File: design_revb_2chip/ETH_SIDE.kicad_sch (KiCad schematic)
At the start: 1 part, among them U2 DP83TG720SWRHARQ1

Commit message: finished initial schematic
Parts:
- added C10, C13, C21, C22, C28: 100nF, symbol Device:C
- added C11, C14, C23, C24, C30: 10nF, symbol Device:C
- added C12, C19, C20, C26: 2.2uF, symbol Device:C
- added C15, C18, C25, C9: 1uF, symbol Device:C
- added C16, C17: 10uF, symbol Device:C
- added C27, C29: 0.1uF, symbol Device:C
- added C31: 4.7nF, symbol Device:C
- added D1, D2, D3: LED, symbol Device:LED
- added FL1, FL2, FL3: BLM18KG601SH1D, BLM18KG601SH1D:BEADC1608X95N, symbol Capstone_Synbols:BLM18KG601SH1D
- added FL4: DLW32MH101XT2L, DLW32MH101XT2L:FIL_DLW32MH101XT2L, symbol Capstone_Synbols:DLW32MH101XT2L
- added J2: 09452812810, 09452812810, symbol Capstone_Synbols:09452812810
- added JP1, JP2, JP5: Jumper_2_Open, symbol Jumper:Jumper_2_Open
- added JP3, JP4: Jumper_2_Bridged, symbol Jumper:Jumper_2_Bridged
- added R10, R11, R12, R14, R15, R18: 2.49k, symbol Device:R_US
- added R13, R16, R17: 470, symbol Device:R_US
- added R5: 10k, symbol Device:R_US
- added R6, R7: 1k, symbol Device:R_US
- added R8: 100k, symbol Device:R_US
- added R9: 2.2k, symbol Device:R_US
- added U5: TPS784105QWDRBRQ1, DRB0008J-IPC_A, symbol Capstone_Synbols:TPS784105QWDRBRQ1
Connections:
- net MDC: now reaches U2.1
- net at U2.10: now also R5.1
- net Vdda3p3: now reaches U2.11
- net Vdda3p3: now also U2.7, U2.8, C26.2, C28.2, C30.2, FL3.2
- net TRD_P: now reaches U2.12
- net TRD_P: now also FL4.1
- net TRD_M: now reaches U2.13
- net TRD_M: now also FL4.4
- net RX_CTRL: now reaches U2.15
- net Vdd1p0A: now reaches U2.21
- net Vdd1p0A: now also U2.9, C19.2, C20.1, C21.2, C22.1, C23.2, C24.1, FL2.2
- net VddioA: now reaches U2.22
- net VddioA: now also U2.34, C10.1, C11.1, C12.2, C13.2, C14.2, FL1.2
- net RX_D3: now reaches U2.23
- net RX_D2: now reaches U2.24
- net RX_D2: now also JP3.1 (A)
- net RX_D1: now reaches U2.25
- net RX_D1: now also JP2.1 (A)
- net RX_D0: now reaches U2.26
- net RX_D0: now also JP1.1 (A)
- net RX_CLK: now reaches U2.27
- net TX_CLK: now reaches U2.28
- net TX_CTRL: now reaches U2.29
- net TX_D3: now reaches U2.30
- net TX_D2: now reaches U2.31
- net TX_D1: now reaches U2.32
- net TX_D0: now reaches U2.33
- net LED_0: now reaches U2.35
- net LED_0: now also JP4.1 (A), JP5.1 (A)
- net MDIO: now reaches U2.36
- net MDIO: now also R9.2
- net CLK_IN: now reaches U2.5
- net LED_1: now reaches U2.6
- net LED_1: now also D3.2 (A), R18.1
- new net: D1.2 (A), JP4.2 (B), R14.1
- new net: JP3.2 (B), R12.2
- new net: C27.1, FL4.2
- new net: C27.2, J2.1 (BI_DA+), R6.1
- new net: D3.1 (K), R17.2
- new net: JP1.2 (B), R10.2
- new net: D2.1 (K), JP5.2 (B), R15.1
- new net: D2.2 (A), R16.1
- new net: C29.1, J2.2 (BI_DA-), R7.1
- new net: C31.1, R6.2, R7.2, R8.1
- new net: JP2.2 (B), R11.2
- new net: C29.2, FL4.3
- new net: D1.1 (K), R13.2
- new net GND: C10.2, C11.2, C12.1, C13.1, C14.1, C15.1, C16.1, C17.1, C18.2, C19.1, C20.2, C21.1, C22.2, C23.1, C24.2, C25.2, C26.1, C28.1, C30.1, C31.2, C9.2, J2.3 (GND_1), J2.4 (GND_2), J2.5 (GND_3), J2.6 (GND_4), R13.1, R14.2, R17.1, R18.2, R5.2, R8.2, R9.1, U5.5 (GND)
- new net Vdd: C15.2, C17.2, C25.1, C9.1, FL1.1, FL3.1, R10.1, R11.1, R12.1, R15.2, R16.2, U5.6 (EN), U5.8 (IN)
- new net Vdd1.0: C16.2, C18.1, FL2.1, U5.1 (OUT)
- no-connect marks 0 -> 13
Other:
- moved on the sheet: U2

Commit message: ready to merge
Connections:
- net GND: now also U2.37
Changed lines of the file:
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@@
+	)
+	(symbol
+		(lib_id "power:GND")
+		(at 77.47 30.48 90)
+		(unit 1)
+		(exclude_from_sim no)
+		(in_bom yes)
+		(on_board yes)
+		(dnp no)
+		(fields_autoplaced yes)
+		(property "Reference" "#PWR044"
+			(at 83.82 30.48 0)
+			(effects
+				(font
+					(size 1.27 1.27)
+				)
+				(hide yes)
+			)
+		)
+		(property "Value" "GND"
+			(at 81.28 30.4799 90)
+			(effects
+				(font
+					(size 1.27 1.27)
+				)
+				(justify right)
+			)
+		)
+		(property "Footprint" ""
+			(at 77.47 30.48 0)
+			(effects
+				(font
+					(size 1.27 1.27)
+				)
+				(hide yes)
+			)
+		)
+		(property "Datasheet" ""
+			(at 77.47 30.48 0)
+			(effects
+				(font
+					(size 1.27 1.27)
+				)
+				(hide yes)
+			)
+		)
+		(property "Description" "Power symbol creates a global label with name \"GND\" , ground"
+			(at 77.47 30.48 0)
+			(effects
+				(font
+					(size 1.27 1.27)
+				)
+				(hide yes)
+			)
+		)
+		(pin "1"
+		)
+		(instances
+			(project ""
+				(path "/d77d37fa-bfdc-44bb-83cc-90773a88d214/0a9cb67f-25c5-4666-b67f-a9781d94061d"
+					(reference "#PWR044")
+					(unit 1)
+				)
+			)
+		)
 	)
 	(symbol

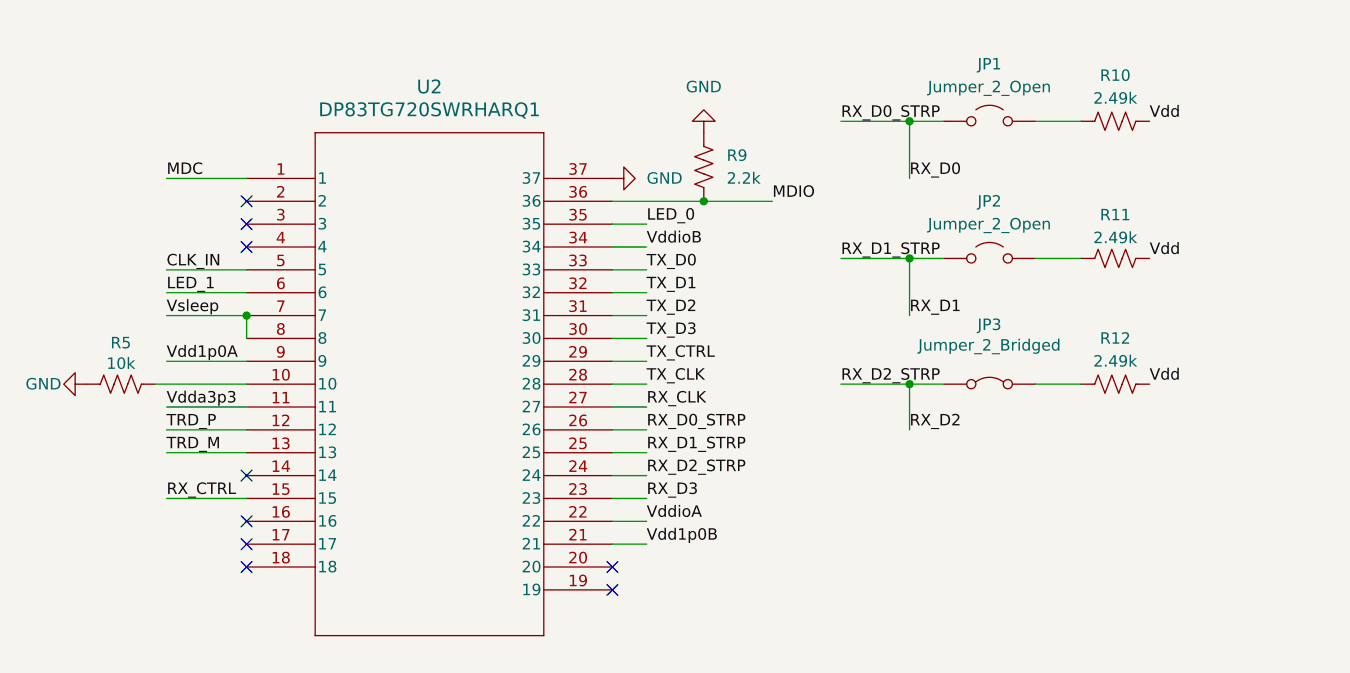
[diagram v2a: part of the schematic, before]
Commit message: Small Fixes
Modifying both pages to try and resolve differences in pins
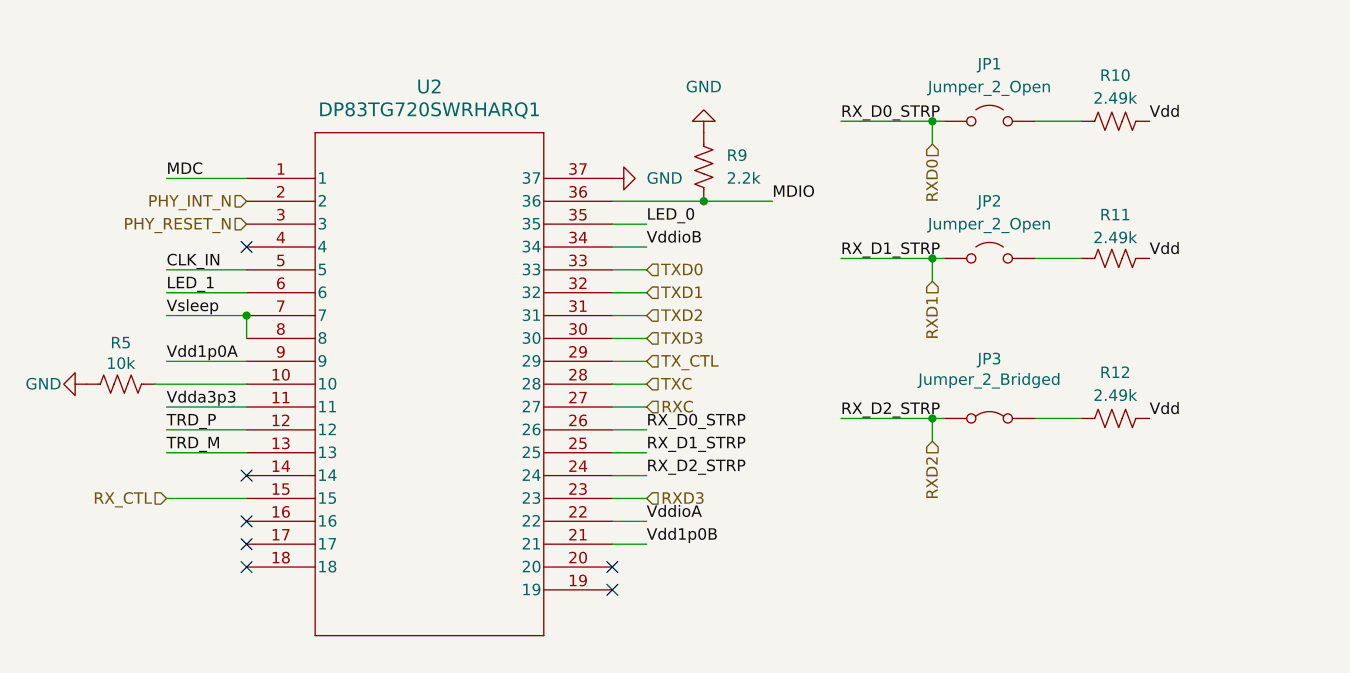
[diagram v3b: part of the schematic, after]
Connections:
- net PHY_INT_N: now reaches U2.2
- net PHY_RESET_N: now reaches U2.3
- net RX_CLK renamed RXC
- net RX_CTRL renamed RX_CTL
- net RX_D0 renamed RXD0
- net RX_D1 renamed RXD1
- net RX_D2 renamed RXD2
- net RX_D3 renamed RXD3
- net TX_CLK renamed TXC
- net TX_CTRL renamed TX_CTL
- net TX_D0 renamed TXD0
- net TX_D1 renamed TXD1
- net TX_D2 renamed TXD2
- net TX_D3 renamed TXD3
- no-connect marks 13 -> 11
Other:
- moved on the sheet: JP3, R12

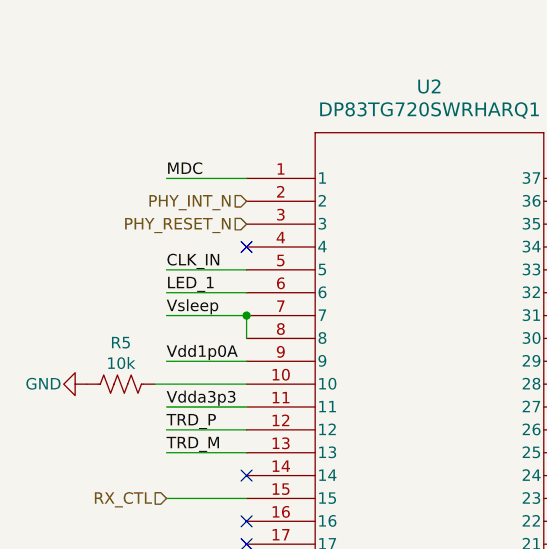
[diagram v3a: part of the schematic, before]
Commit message: Pin Renames
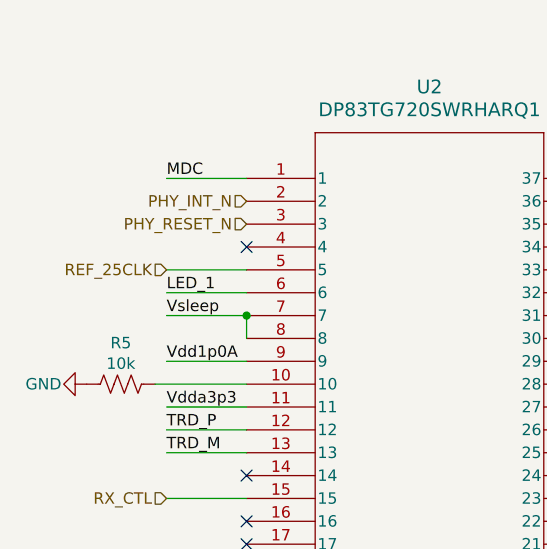
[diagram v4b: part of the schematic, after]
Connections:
- net CLK_IN renamed REF_25CLK
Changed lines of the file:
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@@
-		)
-	)
-	(label "CLK_IN"
-		(at 27.94 40.64 0)
-		(fields_autoplaced yes)
-		(effects
-			(font
-				(size 1.27 1.27)
-			)
-			(justify left bottom)
 		)
 	)
@@
 		(fields_autoplaced yes)
 		(effects
+			(font
+				(size 1.27 1.27)
+			)
+			(justify right)
+		)
+	)
+	(hierarchical_label "REF_25CLK"
+		(shape input)
+		(at 27.94 40.64 180)
+		(fields_autoplaced yes)
+		(effects

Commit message: Annotation
Quick Annotation Update before PCB
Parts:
- renumbered C29 to C28, C31 to C29, C9 to C30, C18 to C31, C25 to C32, C17 to C33, C15 to C34, C12 to C35, C10 to C36, C19 to C37, C20 to C38, C26 to C39, C13 to C40, C21 to C41, C22 to C42, C28 to C43, C11 to C44, C14 to C45, C23 to C46, C24 to C47, C30 to C48, C16 to C49, D2 to D3, D3 to D4, D1 to D5, FL4 to FL1, FL1 to FL2, FL2 to FL3, FL3 to FL4, J2 to J3, JP4 to JP1, JP5 to JP2, JP1 to JP3, JP2 to JP4, JP3 to JP5, R5 to R16, R6 to R17, R7 to R18, R8 to R19, R9 to R20, R15 to R21, R17 to R22, R16 to R23, R18 to R24, R13 to R25, R14 to R26, R10 to R27, R11 to R28, R12 to R29, U2 to U4

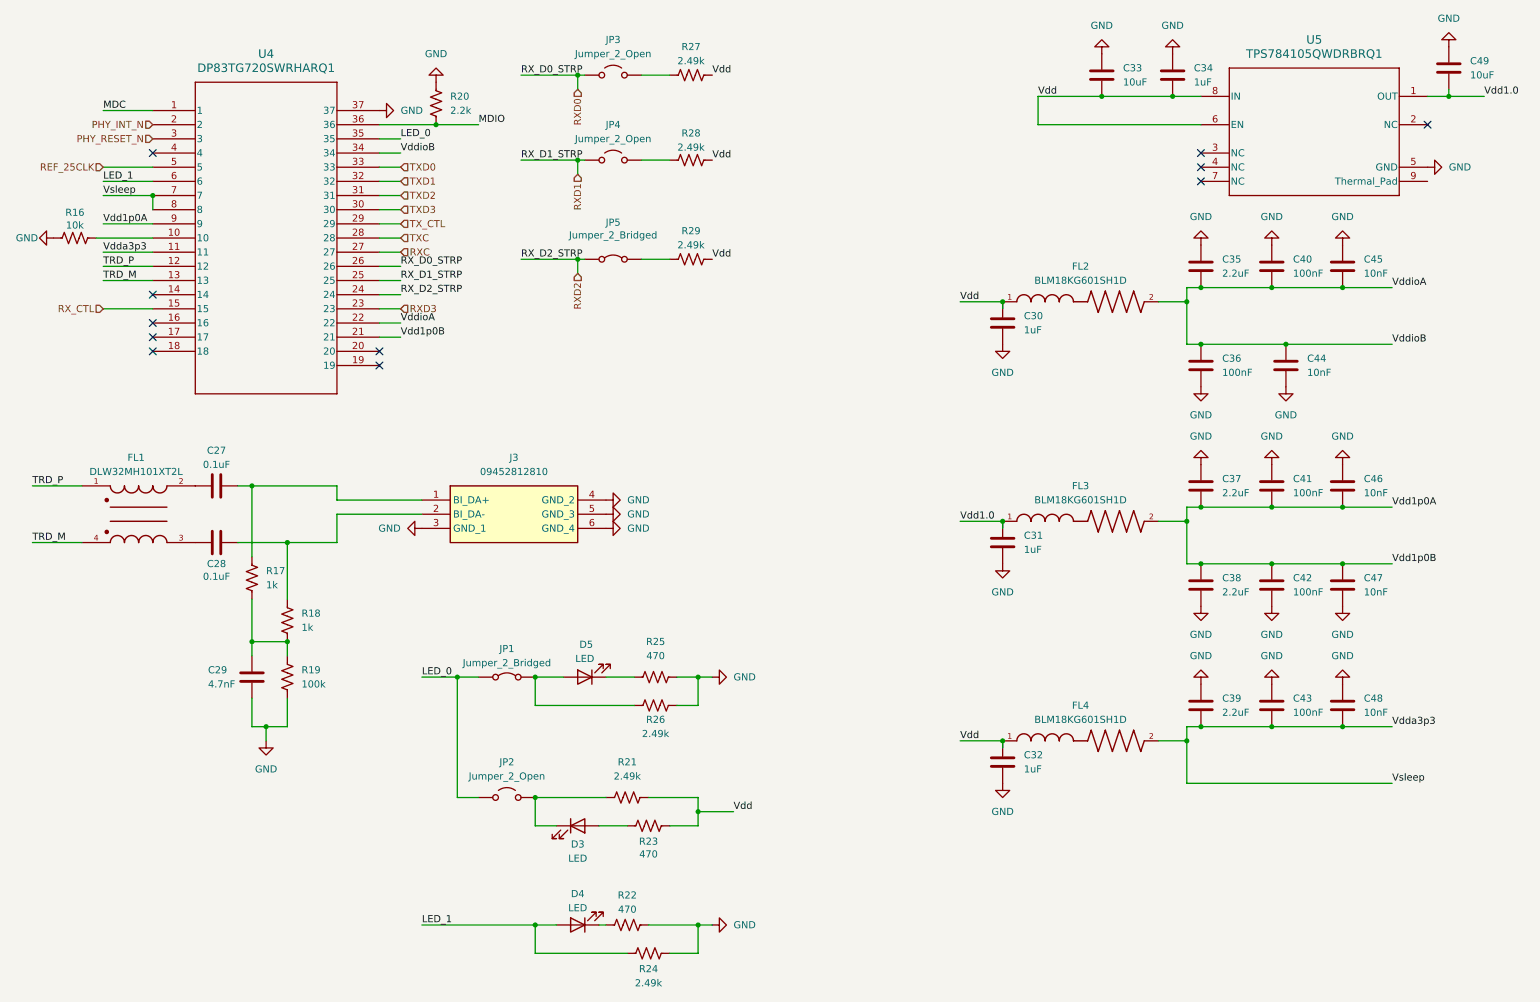
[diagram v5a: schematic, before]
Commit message: ground orientation + resistor tolerances
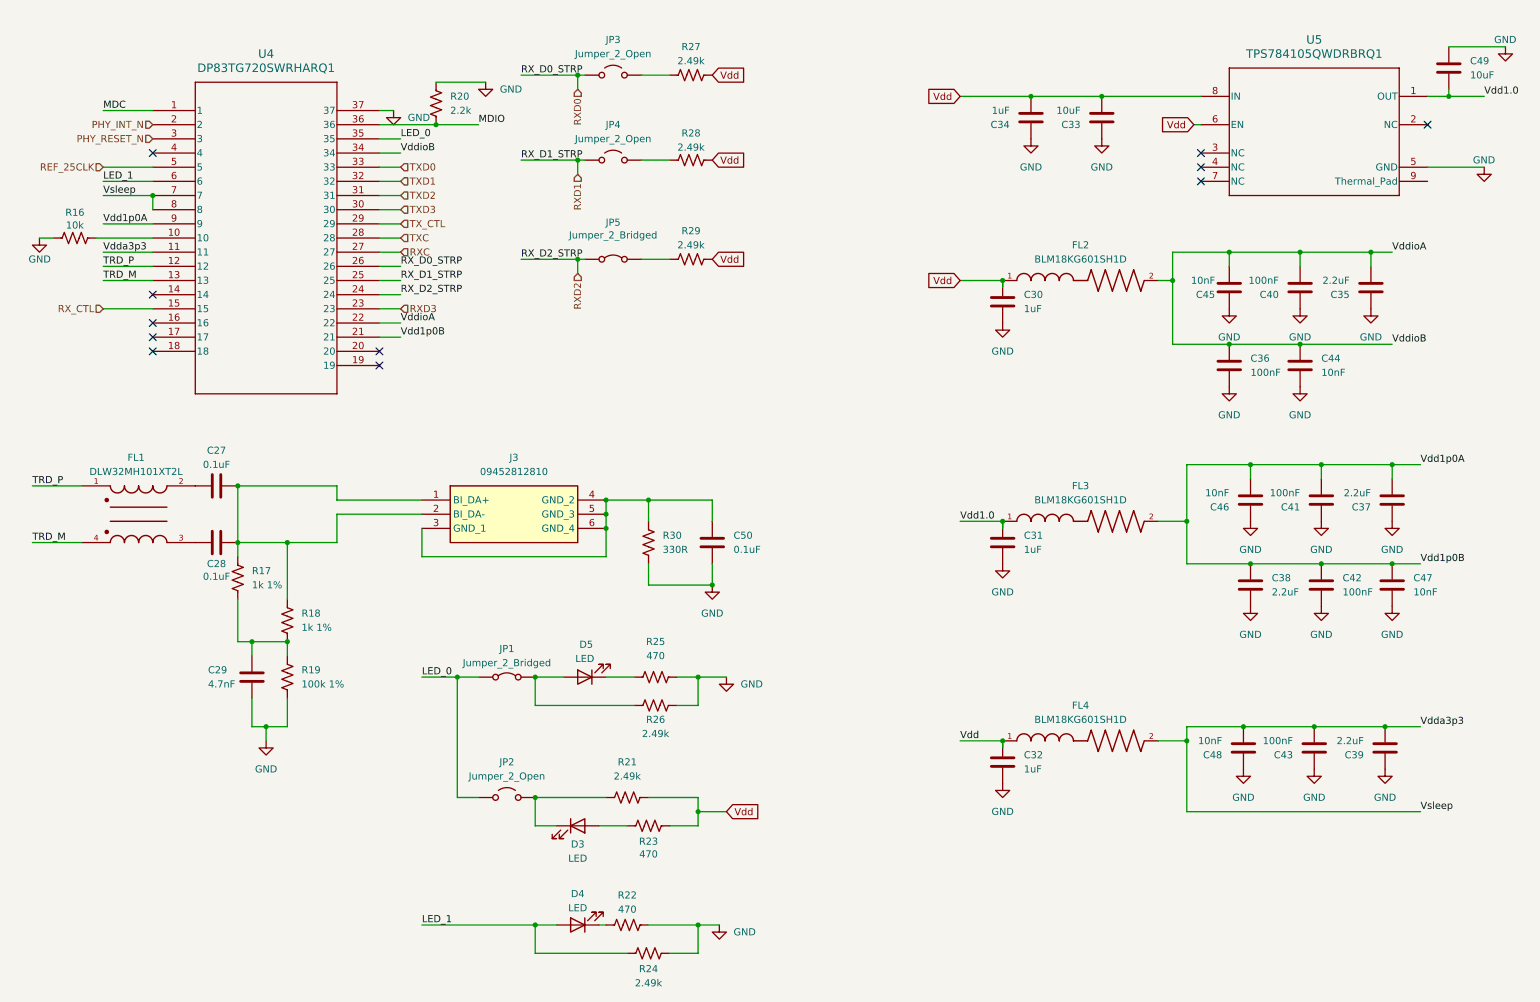
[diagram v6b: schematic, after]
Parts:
- added C50: 0.1uF, symbol Device:C
- added R30: 330R, symbol Device:R_US
- R17, R18: value 1k -> 1k 1%
- R19: value 100k -> 100k 1%
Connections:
- net GND: now also C50.2, R30.1; no longer J3.3 (GND_1), J3.4 (GND_2), J3.5 (GND_3), J3.6 (GND_4)
- net at C27.2, J3.1 (BI_DA+), R17.1: now also C28.1, J3.2 (BI_DA-), R18.1
- new net: C50.1, J3.3 (GND_1), J3.4 (GND_2), J3.5 (GND_3), J3.6 (GND_4), R30.2
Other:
- moved on the sheet: C30, C33, C34, C35, C36, C37, C38, C39, C40, C41, C42, C43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
